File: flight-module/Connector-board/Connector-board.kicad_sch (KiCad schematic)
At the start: 16 parts, among them J10 Pin Jumper, J13 Conn_01x08_Male, J18 Conn_01x02_Male, J19 Conn_01x02_Male, J20 Conn_01x02_Male, J6 ESP32-DEVKITC-32D, J7 Conn_01x19_Male, J9 Conn_01x19_Male, SW1 SW_SPST, U2 74HC4050D, U3 XTSD04GLGEAG, U5 PCF8575DW

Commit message: skeleton for connector board
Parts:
- removed J10: Pin Jumper, Connector_PinHeader_2.54mm:PinHeader_1x02_P2.54mm_Vertical, symbol Connector:Conn_01x02_Male
- removed J13: Conn_01x08_Male, Connector_PinHeader_2.54mm:PinHeader_1x08_P2.54mm_Vertical, symbol Connector:Conn_01x08_Male
- removed J18, J19, J20: Conn_01x02_Male, Connector_PinHeader_2.54mm:PinHeader_1x02_P2.54mm_Vertical, symbol Connector:Conn_01x02_Male
- removed J6: ESP32-DEVKITC-32D, Ellie_Project_Footprints:MODULE_ESP32-DEVKITC-32D, symbol ESP32:ESP32-DEVKITC-32D
- removed J7, J9: Conn_01x19_Male, Connector_PinHeader_2.54mm:PinHeader_1x19_P2.54mm_Vertical, symbol Connector:Conn_01x19_Male
- removed R2: 1k, Resistor_SMD:R_0603_1608Metric, symbol Device:R_Small
- removed R4, R5, R6: 10k, Resistor_SMD:R_0603_1608Metric, symbol Device:R_Small
- removed SW1: SW_SPST, Button_Switch_THT:SW_PUSH_6mm, symbol Switch:SW_SPST
- removed U2: 74HC4050D, 74HC4050D:SO16, symbol Buf_74HC4050D:74HC4050D
- removed U3: XTSD04GLGEAG, XTSD04GLGEAG:SON127P600X800X95-8N, symbol XTSD_NAND:XTSD04GLGEAG
- removed U5: PCF8575DW, PCF8575DW:SOIC127P1030X265-24N, symbol PCF8575DW:PCF8575DW
- added J? (x3): DB15_Female, symbol Connector:DB15_Female
- added J? (x2): Stack_Shape, symbol Stack_Shape:Stack_Shape
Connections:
- no-connect marks 41 -> 0
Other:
- note removed: "ESP32"
- note removed: "SD Card"

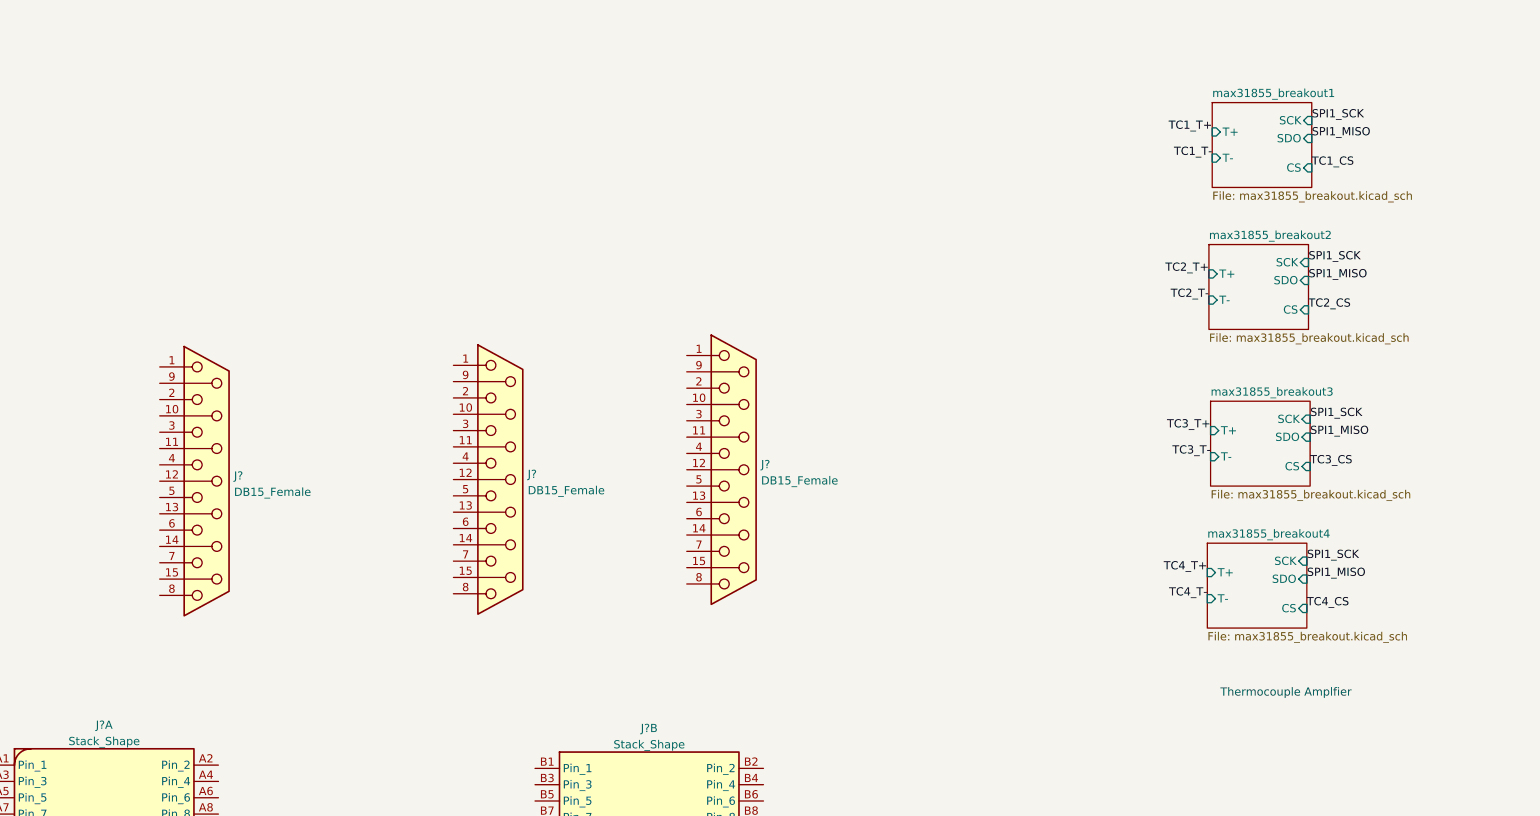
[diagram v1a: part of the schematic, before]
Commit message: worked on core-board schematic. Not done.
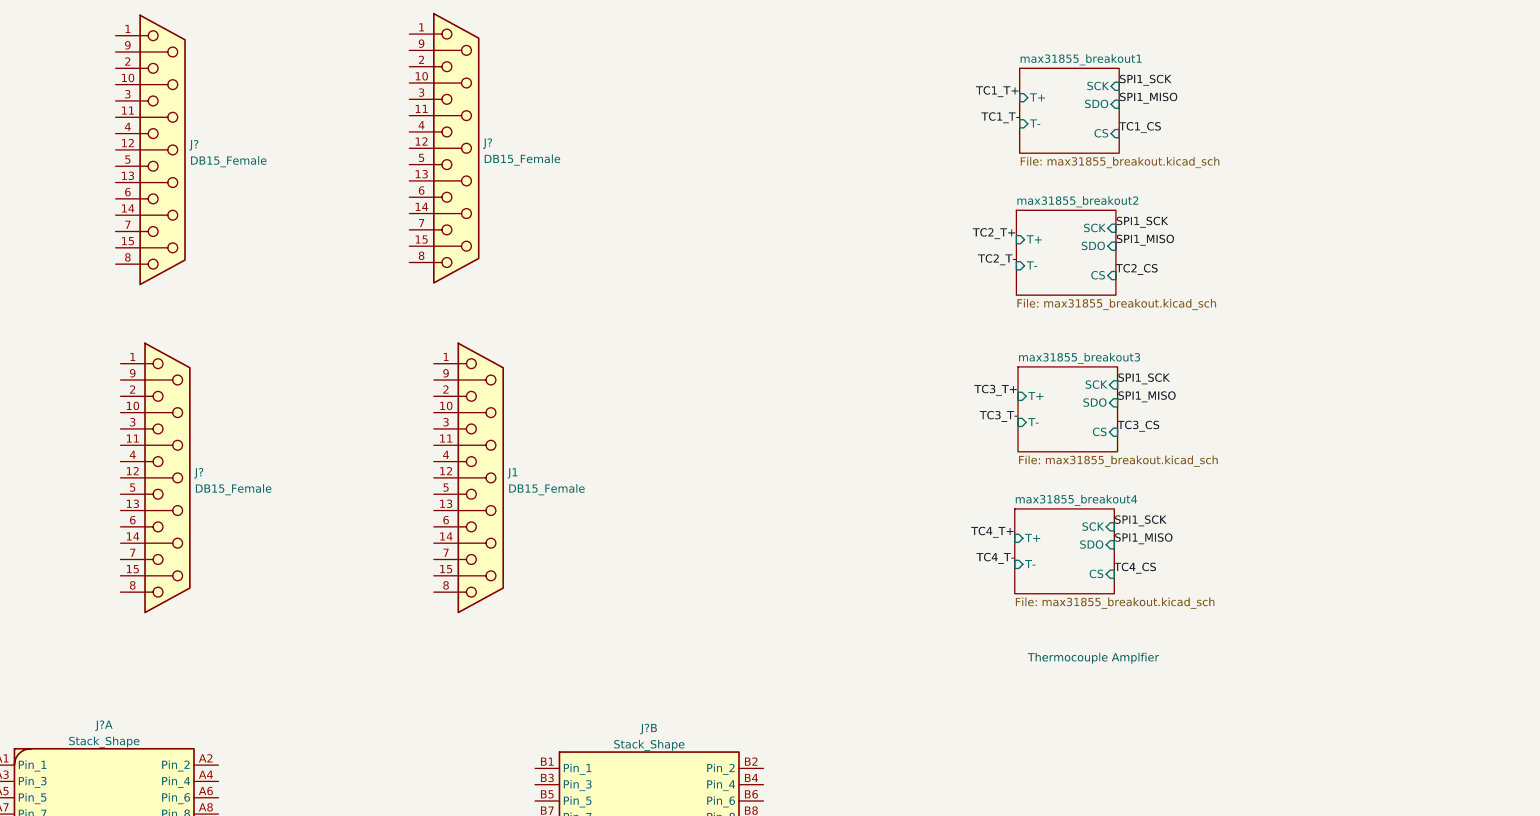
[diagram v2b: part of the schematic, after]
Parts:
- added J1: DB15_Female, symbol Connector:DB15_Female
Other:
- moved on the sheet: J?

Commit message: commit
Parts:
- gave numbers to parts that had none: 4
- renumbered J1 to J5
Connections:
- net TC1_T+: now also J3.3
- net TC1_T-: now also J3.10 (P10)
- net TC2_T+: now also J3.4
- net TC2_T-: now also J3.11 (P111)
- net TC3_T+: now also J3.5
- net TC3_T-: now also J3.12 (P12)
- net TC4_T+: now also J3.6
- net TC4_T-: now also J3.13 (P13)
- net PWR SUP 1+: now reaches J2.1
- net PWR SUP 2-: now reaches J2.10 (P10)
- net PWR SUP 2-: now also J2.11 (P111)
- net REDS-GND: now reaches J2.12 (P12)
- net REDS-ETH Vent: now reaches J2.13 (P13)
- net REDS-LOX Vent: now reaches J2.14 (P14)
- net PWR SUP 2+: now reaches J2.2
- net PWR SUP 2+: now also J2.3
- net GND-ETH Main: now reaches J2.4
- net GND-ETH Vent: now reaches J2.5
- net GND-LOX Vent: now reaches J2.6
- net PWR SUP 1-: now reaches J2.9 (P9)
- net LOX_VENT +: now reaches J5.1
- net ETH_MAIN -: now reaches J5.10 (P10)
- net ETH_VENT -: now reaches J5.11 (P111)
- net EXTRA -: now reaches J5.12 (P12)
- net ETH_MAIN +: now reaches J5.2
- net ETH_VENT +: now reaches J5.3
- net EXTRA +: now reaches J5.4
- net LOX_VENT-: now reaches J5.9 (P9)
- net PT6_A+: now reaches J3.1
- net PT6_E-: now reaches J3.2
- net PT6_E+: now reaches J3.9 (P9)
- net PT1_E+: now reaches J4.1
- net PT2_E-: now reaches J4.10 (P10)
- net PT2_A+: now reaches J4.11 (P111)
- net PT3_A+: now reaches J4.12 (P12)
- net PT4_E-: now reaches J4.13 (P13)
- net PT4_A+: now reaches J4.14 (P14)
- net PT5_A+: now reaches J4.15 (P15)
- net PT1_E-: now reaches J4.2
- net PT2_E+: now reaches J4.3
- net PT3_E+: now reaches J4.4
- net PT3_E-: now reaches J4.5
- net PT5_E+: now reaches J4.7
- net PT5_E-: now reaches J4.8
- net PT1_A+: now reaches J4.9 (P9)

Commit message: commit
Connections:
- net PT1_A+: now also J1.B15 (Pin_15)
- net PT1_E+: now also J1.B11 (Pin_11)
- net PT1_E-: now also J1.B13 (Pin_13)
- net PT2_A+: now also J1.B23 (Pin_23)
- net PT2_E+: now also J1.B19 (Pin_19)
- net PT2_E-: now also J1.B21 (Pin_21)
- net PT3_A+: now also J1.B31 (Pin_31)
- net PT3_E+: now also J1.B27 (Pin_27)
- net PT3_E-: now also J1.B29 (Pin_29)
- net PT4_A+: now also J1.B39 (Pin_39)
- net PT4_E+: now also J1.B35 (Pin_35)
- net PT4_E-: now also J1.B37 (Pin_37)
- net PT5_A+: now also J1.B32 (Pin_32)
- net PT5_E+: now also J1.B28 (Pin_28)
- net PT5_E-: now also J1.B30 (Pin_30)
- net PT6_A+: now also J1.B40 (Pin_40)
- net PT6_E+: now also J1.B36 (Pin_36)
- net PT6_E-: now also J1.B38 (Pin_38)
- net PWR SUP 1+: now also J1.A27 (Pin_27), J1.A28 (Pin_28), J1.A29 (Pin_29), J1.A30 (Pin_30), J1.A31 (Pin_31), J1.A32 (Pin_32)
- net PWR SUP 2+: now also J1.A35 (Pin_35), J1.A36 (Pin_36), J1.A37 (Pin_37), J1.A38 (Pin_38), J1.A39 (Pin_39), J1.A40 (Pin_40)
- net PWR SUP 2-: now also J1.A3 (Pin_3), J1.A4 (Pin_4)
- net SPI1_MISO: now also J1.B4 (Pin_4)
- net SPI1_SCK: now also J1.B2 (Pin_2)
- net TC1_CS: now also J1.B10 (Pin_10)
- net TC2_CS: now also J1.B12 (Pin_12)
- net TC3_CS: now also J1.B16 (Pin_16)
- net TC4_CS: now also J1.B18 (Pin_18)
- net 3v3: now reaches J1.A1 (Pin_1)
- net 3v3: now also J1.A2 (Pin_2)
- net GND2: now reaches J1.A10 (Pin_10)
- net GND2: now also J1.A13 (Pin_13), J1.A14 (Pin_14), J1.A17 (Pin_17), J1.A18 (Pin_18), J1.A21 (Pin_21), J1.A22 (Pin_22), J1.A25 (Pin_25), J1.A26 (Pin_26), J1.A33 (Pin_33), J1.A34 (Pin_34), J1.A9 (Pin_9)
- net LOX_VENT: now reaches J1.A11 (Pin_11)
- net LOX_VENT: now also J1.A12 (Pin_12)
- net ETH_VENT: now reaches J1.A15 (Pin_15)
- net ETH_VENT: now also J1.A16 (Pin_16)
- net ETH_MAIN: now reaches J1.A19 (Pin_19)
- net ETH_MAIN: now also J1.A20 (Pin_20)
- net GND1: now reaches J1.B14 (Pin_14)
- net GND1: now also J1.B17 (Pin_17), J1.B20 (Pin_20), J1.B25 (Pin_25), J1.B26 (Pin_26), J1.B33 (Pin_33), J1.B34 (Pin_34), J1.B5 (Pin_5), J1.B8 (Pin_8), J1.B9 (Pin_9)
- no-connect marks 0 -> 25

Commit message: update on flight pcbs
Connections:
- net 3v3 is gone; now on net +3.3V: J1.A1 (Pin_1), J1.A2 (Pin_2)
- net ETH_VENT + is gone; now on net ETH_Vent: J5.3
- net ETH_VENT - is gone; now on net GND2: J5.11 (P111)
- net GND-ETH Vent is gone; now on net ETH_Vent: J2.5
- net GND1 is gone; now on net GND: J1.B14 (Pin_14), J1.B17 (Pin_17), J1.B20 (Pin_20), J1.B25 (Pin_25), J1.B26 (Pin_26), J1.B33 (Pin_33), J1.B34 (Pin_34), J1.B5 (Pin_5), J1.B8 (Pin_8), J1.B9 (Pin_9)
- net LOX_VENT is gone; now on net LOX_Vent: J1.A11 (Pin_11), J1.A12 (Pin_12)
- net LOX_VENT + is gone; now on net LOX_Vent: J5.1
- net LOX_VENT- is gone; now on net GND2: J5.9 (P9)
- net PWR SUP 1- is gone; now on net GND: J2.9 (P9)
- net REDS-ETH Vent is gone; now on net ETH_Vent: J2.13 (P13)
- net REDS-GND is gone; now on net GND2: J2.12 (P12)
- net REDS-LOX Vent is gone; now on net LOX_Vent: J2.14 (P14)
- net GND2: now also J2.10 (P10), J2.11 (P111)
- net PT4_E+: now also J4.6
- net PWR SUP 2-: no longer J2.10 (P10), J2.11 (P111)
- net ETH_MAIN: no longer names the net of J1.A19 (Pin_19)
- net ETH_MAIN: no longer J1.A20 (Pin_20)
- net ETH_MAIN +: no longer names the net of J5.2
- net ETH_MAIN -: no longer names the net of J5.10 (P10)
- net ETH_VENT renamed ETH_Vent
- net EXTRA +: no longer names the net of J5.4
- net EXTRA -: no longer names the net of J5.12 (P12)
- net GND-ETH Main: no longer names the net of J2.4
- net GND-LOX Vent renamed LOX_Vent
- no-connect marks 25 -> 33
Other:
- note added: "Ground_"
- note added: "REDS_"

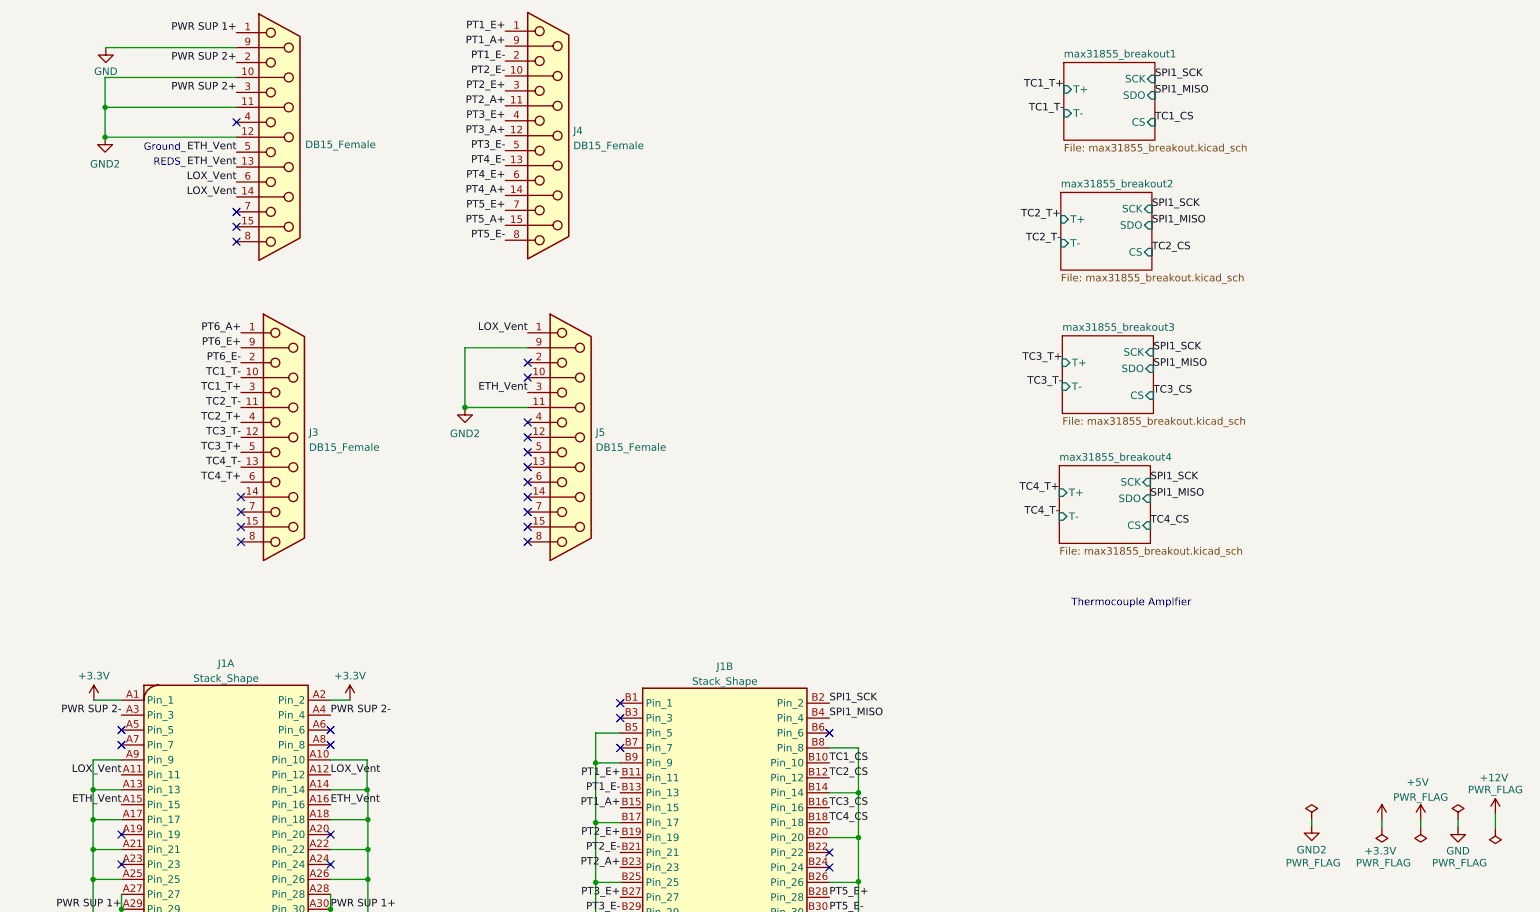
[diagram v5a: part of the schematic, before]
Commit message: added diodes to 'OR' REDS-vent with on-board mosfets.
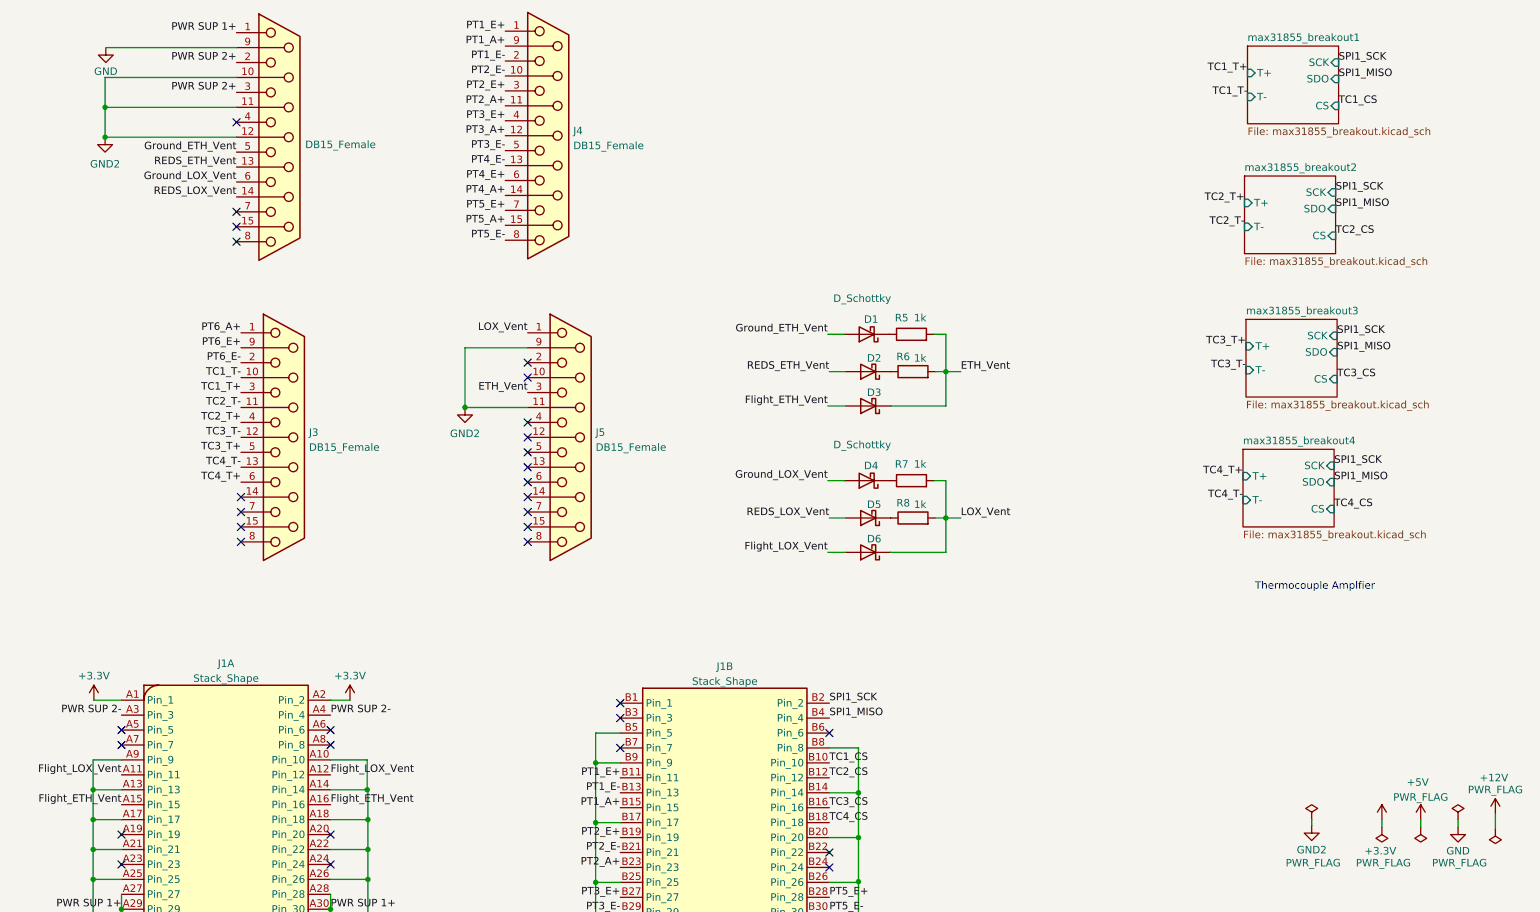
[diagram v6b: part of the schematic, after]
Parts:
- added D1, D2, D3, D4, D5, D6: D_Schottky, symbol Device:D_Schottky
- added R5, R6, R7, R8: 1k, symbol Device:R
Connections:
- net ETH_Vent: now also D3.1 (K), R5.2, R6.2; no longer J1.A15 (Pin_15), J1.A16 (Pin_16), J2.13 (P13), J2.5
- net LOX_Vent: now also D6.1 (K), R7.2, R8.2; no longer J1.A11 (Pin_11), J1.A12 (Pin_12), J2.14 (P14), J2.6
- new net: D5.1 (K), R8.1
- new net: D4.1 (K), R7.1
- new net: D2.1 (K), R6.1
- new net: D1.1 (K), R5.1
- new net Flight_ETH_Vent: D3.2 (A), J1.A15 (Pin_15), J1.A16 (Pin_16)
- new net Flight_LOX_Vent: D6.2 (A), J1.A11 (Pin_11), J1.A12 (Pin_12)
- new net Ground_ETH_Vent: D1.2 (A), J2.5
- new net Ground_LOX_Vent: D4.2 (A), J2.6
- new net REDS_ETH_Vent: D2.2 (A), J2.13 (P13)
- new net REDS_LOX_Vent: D5.2 (A), J2.14 (P14)
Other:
- note removed: "Ground_"
- note removed: "REDS_"

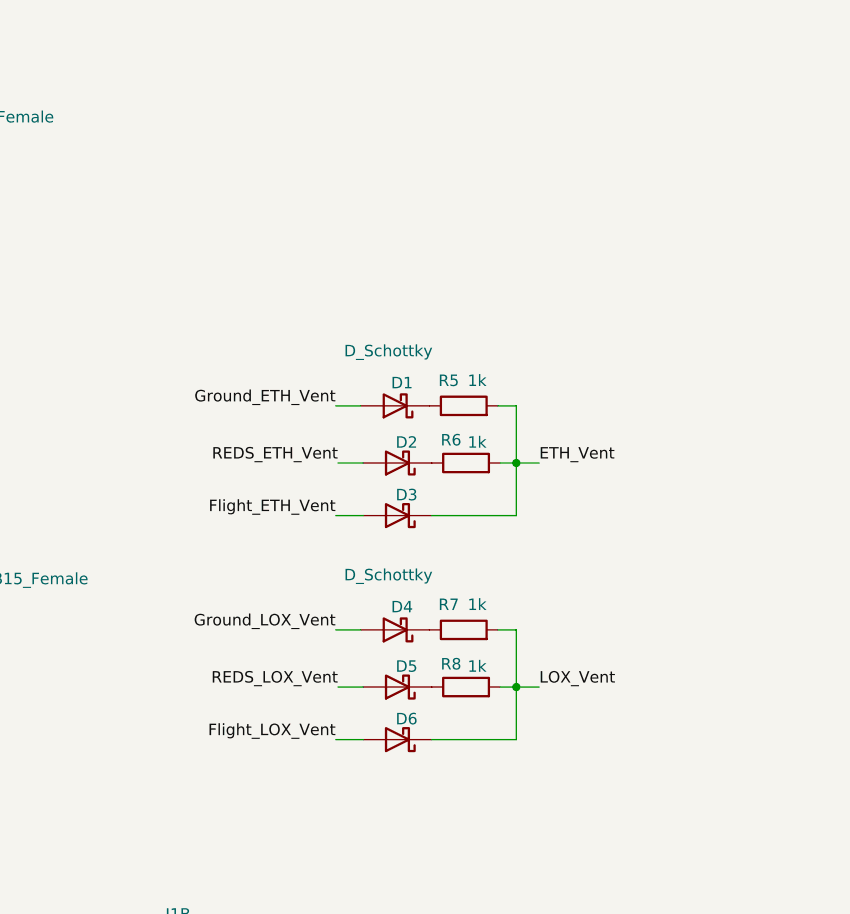
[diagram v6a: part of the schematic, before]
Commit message: Updated power mux circuit.
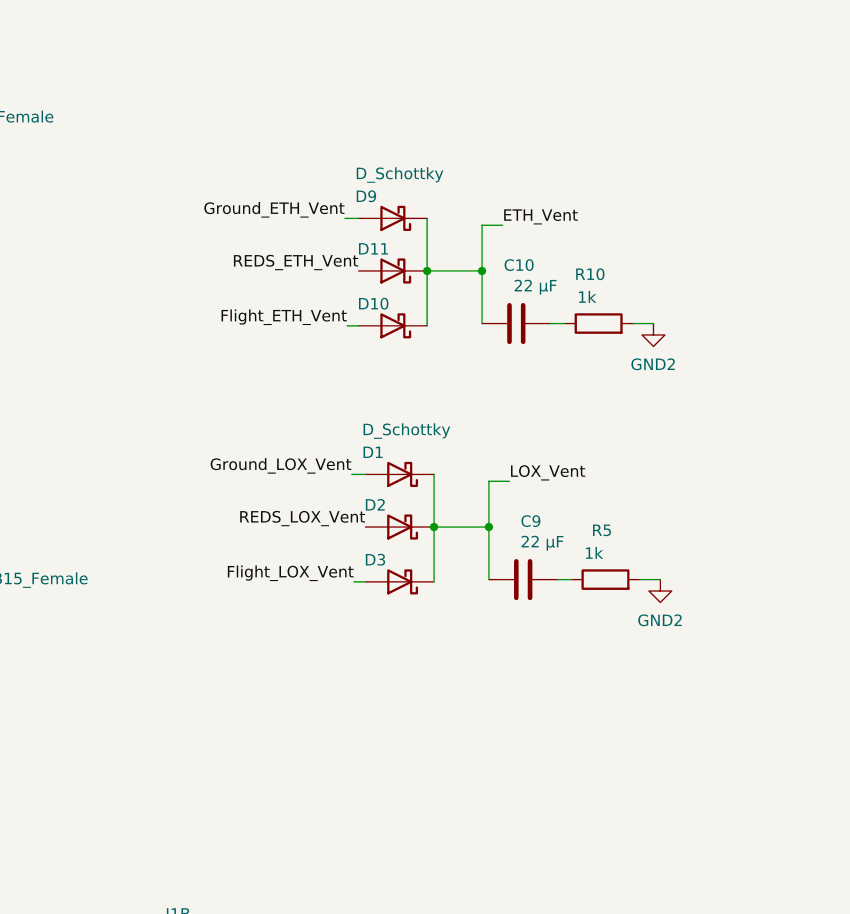
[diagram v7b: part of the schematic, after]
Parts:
- removed D4, D5, D6: D_Schottky, symbol Device:D_Schottky
- removed R6, R7, R8: 1k, symbol Device:R
- added C10, C9: 22 µF, symbol Device:C
- added D10, D11, D9: D_Schottky, symbol Device:D_Schottky
- added R10: 1k, symbol Device:R
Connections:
- net ETH_Vent: now also C10.1, D10.1 (K), D11.1 (K), D9.1 (K); no longer D3.1 (K), R5.2
- net Flight_ETH_Vent: now also D10.2 (A); no longer D3.2 (A)
- net Flight_LOX_Vent: now also D3.2 (A)
- net GND2: now also R5.2, R10.2
- net Ground_ETH_Vent: now also D9.2 (A); no longer D1.2 (A)
- net Ground_LOX_Vent: now also D1.2 (A)
- net LOX_Vent: now also D1.1 (K), D2.1 (K), D3.1 (K), C9.1
- net REDS_ETH_Vent: now also D11.2 (A); no longer D2.2 (A)
- net REDS_LOX_Vent: now also D2.2 (A)
- net at R5.1: now also C9.2; no longer D1.1 (K)
- new net: C10.2, R10.1
